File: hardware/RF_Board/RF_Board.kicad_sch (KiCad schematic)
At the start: 129 parts, among them J1 Conn_Coaxial, J2 Conn_01x07_Male, J3 Conn_Coaxial, J4 Conn_01x07_Male, J5 Conn_01x06_Female, J6 Conn_01x06_Female, J7 Conn_01x06_Female, J9 LD15S33E4GX00LF, Q1 2N7002, Q2 2N7002, U1 MSP430FR2355TPT, U10 QPL9096, U11 QPL9096, U12 74HC04, U13 RFM95PW, U14 TPS259573DSGR, U15 TPS259573DSGR, U2 MSP430FR2355TPT, U3 CC2500, U4 HMC574, U5 HMC574, U6 YAT-5A+, U7 SKY65900-11, U8 LFCN-2750+, U9 DEA202450BT-1213C1, Y1 Crystal_GND24, Y2 Crystal, Y3 Crystal

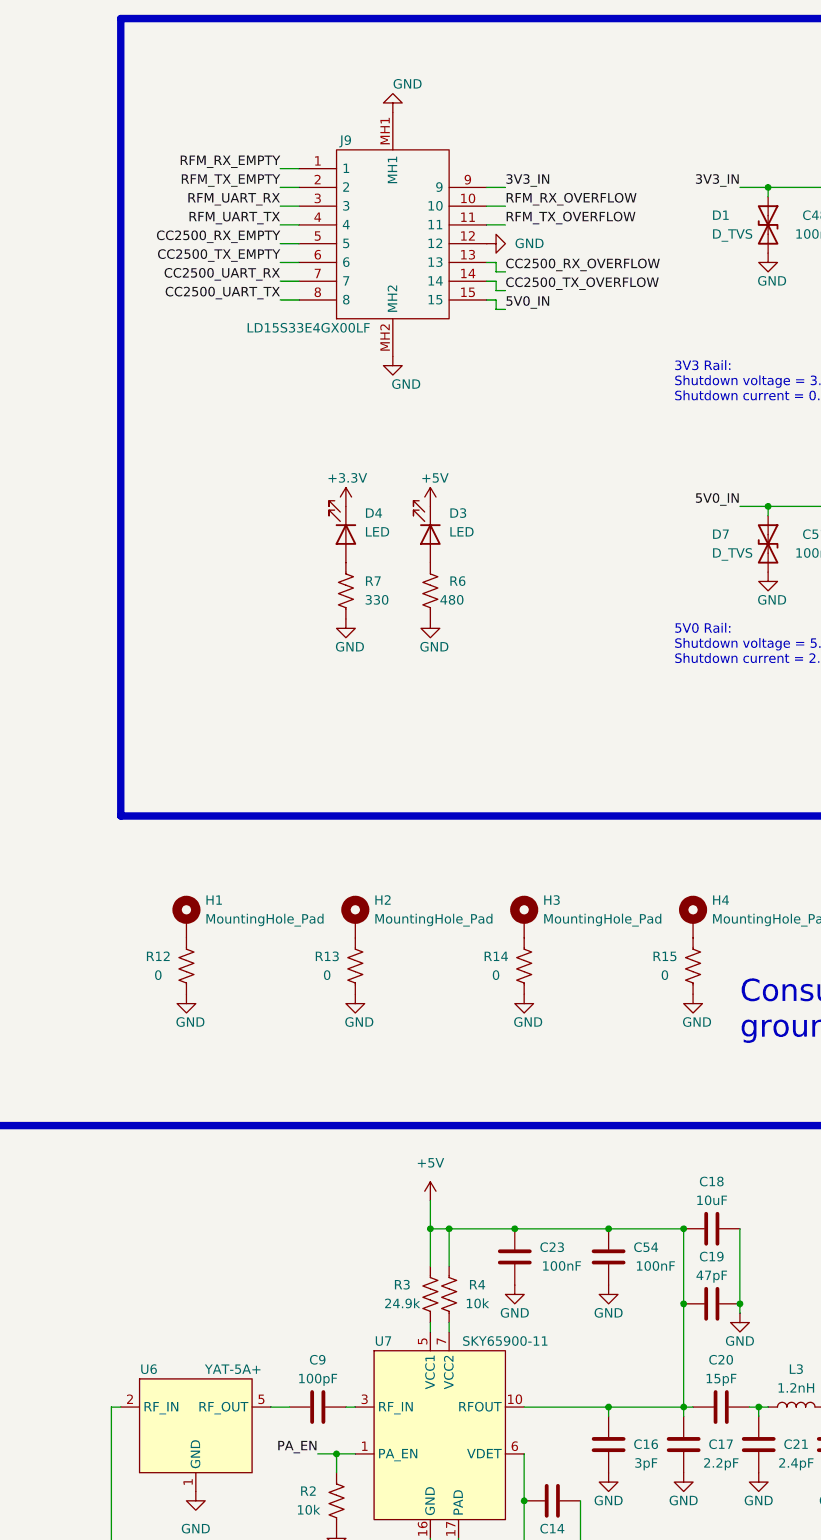
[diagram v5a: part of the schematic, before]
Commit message: more RF board layout
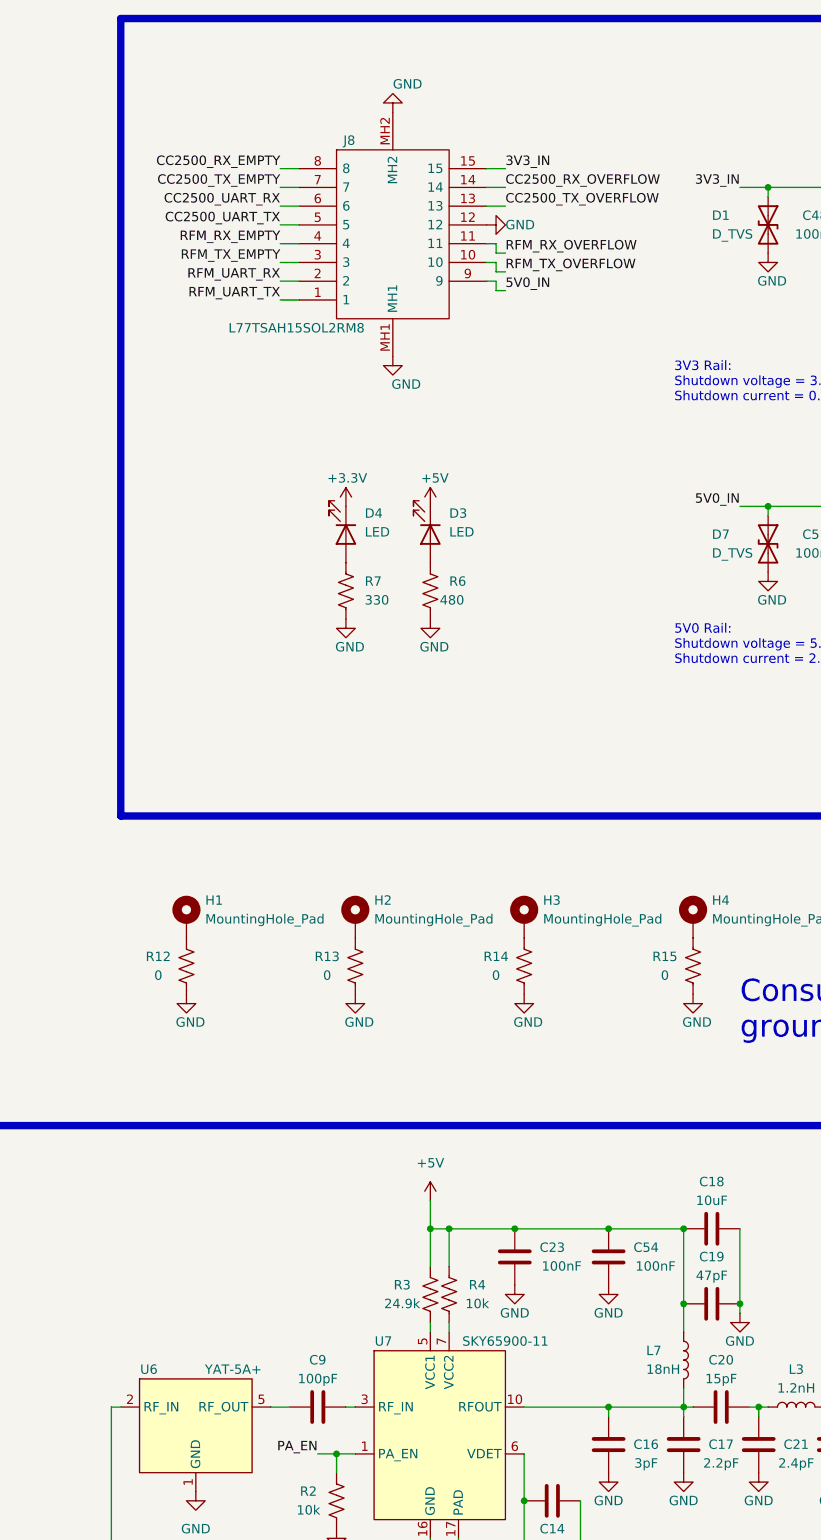
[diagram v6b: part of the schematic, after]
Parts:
- removed J9: LD15S33E4GX00LF, RF_Board_Footprints:LD15S33E4GX00LF, symbol RF_Board_Symbols:LD15S33E4GX00LF
- added J8: L77TSAH15SOL2RM8, L77TSAH15SOL2RM8, symbol RF_Board_Symbols:L77TSAH15SOL2RM8
- added L7: 18nH, RF_Board_Footprints:L_0603_1608Metric, symbol RF_Board_Symbols:L
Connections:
- net +5V: now also L7.1; no longer C16.1, C17.1, C20.1, U7.10 (RFOUT), U7.11 (RFOUT)
- net 3V3_IN: now also J8.15
- net 5V0_IN: now also J8.9
- net CC2500_RX_EMPTY: now also J8.8
- net CC2500_RX_OVERFLOW: now also J8.14
- net CC2500_TX_EMPTY: now also J8.7
- net CC2500_TX_OVERFLOW: now also J8.13
- net CC2500_UART_RX: now also J8.6
- net CC2500_UART_TX: now also J8.5
- net GND: now also J8.12, J8.MH1, J8.MH2
- net RFM_RX_EMPTY: now also J8.4
- net RFM_RX_OVERFLOW: now also J8.11
- net RFM_TX_EMPTY: now also J8.3
- net RFM_TX_OVERFLOW: now also J8.10
- net RFM_UART_RX: now also J8.2
- net RFM_UART_TX: now also J8.1
- new net: C16.1, C17.1, C20.1, L7.2, U7.10 (RFOUT), U7.11 (RFOUT)

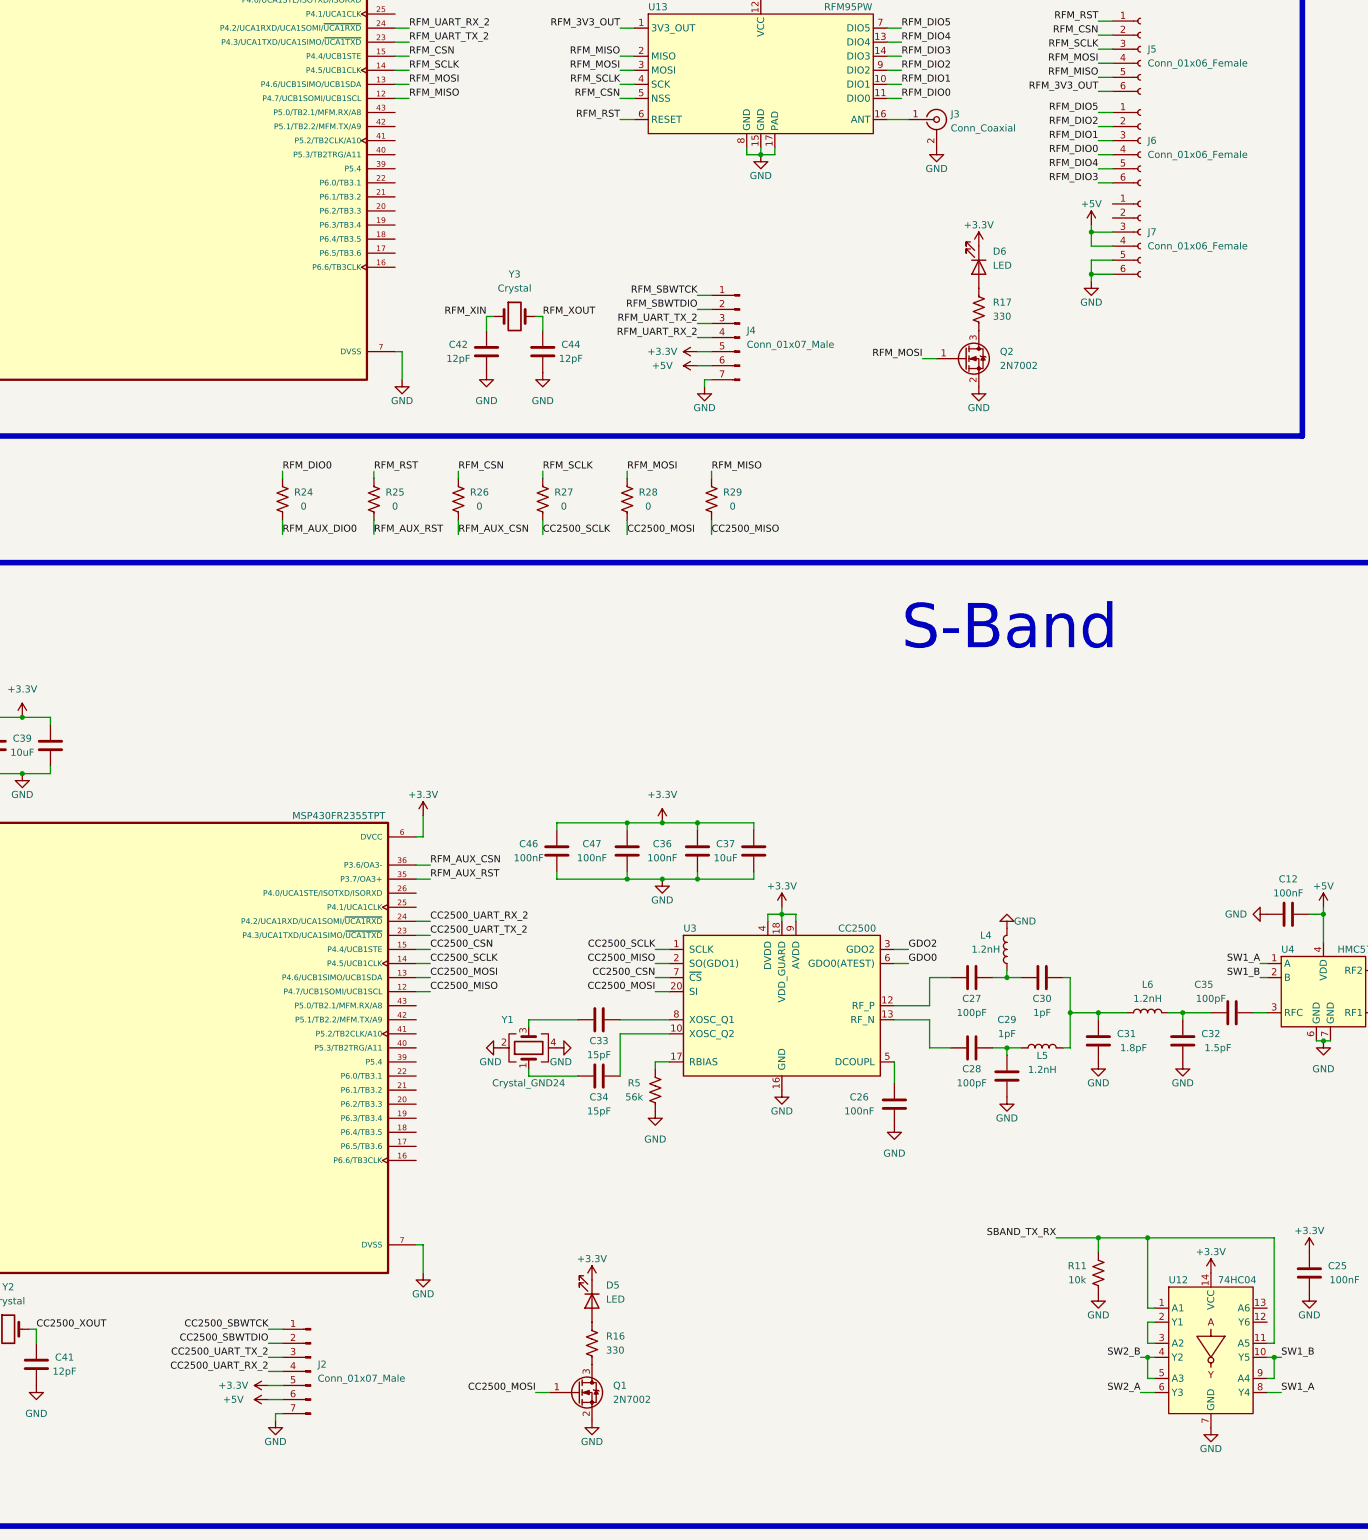
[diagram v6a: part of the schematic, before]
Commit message: add UHF module to RF board
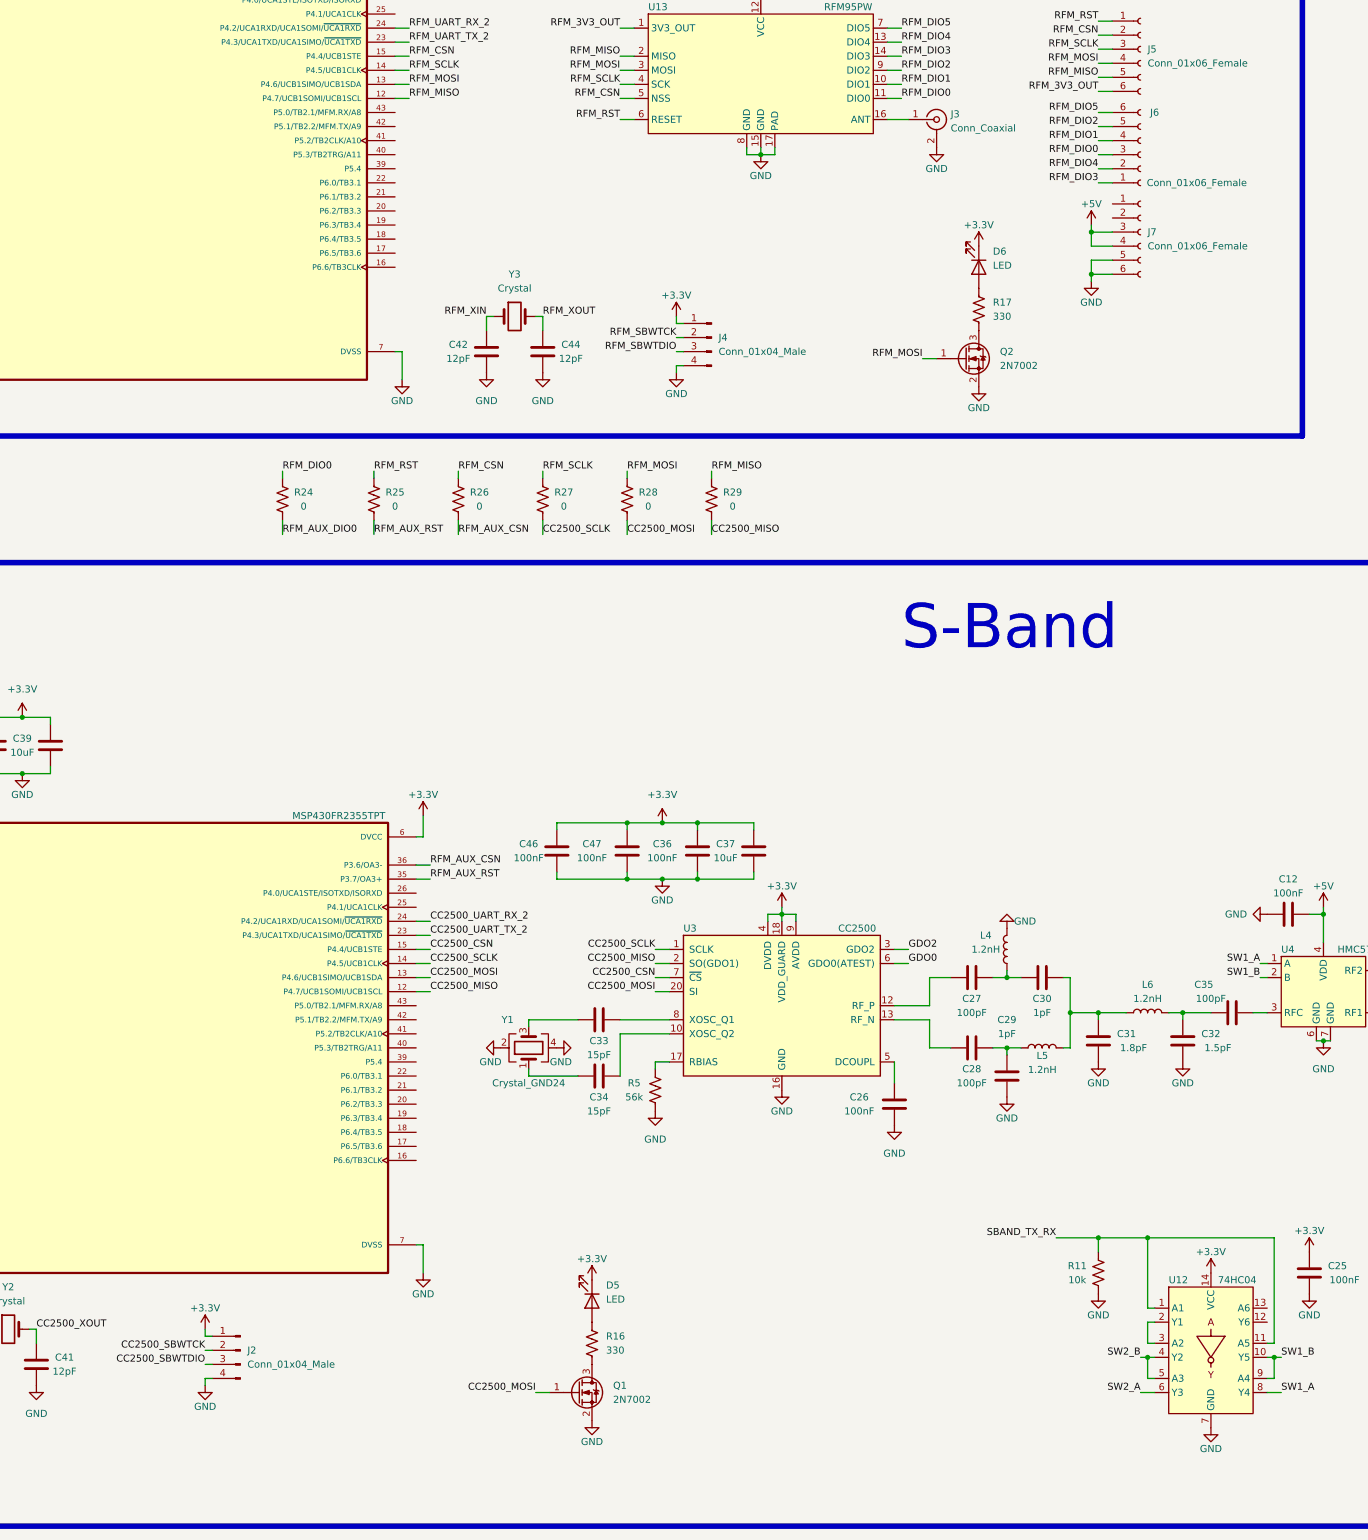
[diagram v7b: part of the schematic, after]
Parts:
- removed J2, J4: Conn_01x07_Male, RF_Board_Footprints:PinHeader_1x07_P2.54mm_Vertical, symbol RF_Board_Symbols:Conn_01x07_Male
- added J2, J4: Conn_01x04_Male, RF_Board_Footprints:PinHeader_1x04_P2.54mm_Vertical, symbol RF_Board_Symbols:Conn_01x04_Male
- U13: footprint (none) -> RF_Board_Footprints:RFM95PW
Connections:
- net +3.3V: now also J2.1 (Pin_1), J4.1 (Pin_1)
- net CC2500_SBWTCK: now also J2.2 (Pin_2)
- net CC2500_SBWTDIO: now also J2.3 (Pin_3)
- net GND: now also J2.4 (Pin_4), J4.4 (Pin_4)
- net RFM_DIO0: now also J6.3 (Pin_3); no longer J6.4 (Pin_4)
- net RFM_DIO1: now also J6.4 (Pin_4); no longer J6.3 (Pin_3)
- net RFM_DIO2: now also J6.5 (Pin_5); no longer J6.2 (Pin_2)
- net RFM_DIO3: now also J6.1 (Pin_1); no longer J6.6 (Pin_6)
- net RFM_DIO4: now also J6.2 (Pin_2); no longer J6.5 (Pin_5)
- net RFM_DIO5: now also J6.6 (Pin_6); no longer J6.1 (Pin_1)
- net RFM_SBWTCK: now also J4.2 (Pin_2)
- net RFM_SBWTDIO: now also J4.3 (Pin_3)
